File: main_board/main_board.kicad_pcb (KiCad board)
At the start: 2 copper layers, 160 x 110 mm, 143 parts, among them IC1 MP2722GRH-0000-Z, IC2 MP3429GL-Z, IC4 TS921ID, IC5 CY7C65632-28LTXC, IC6 TS921ID, J1 USB3_A, J10 Conn_01x22_Female, J11 501568-0607-TR325, J12 SM04B-XSRS-ETBLFSN, J13 SM10B-XSRS-ETB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

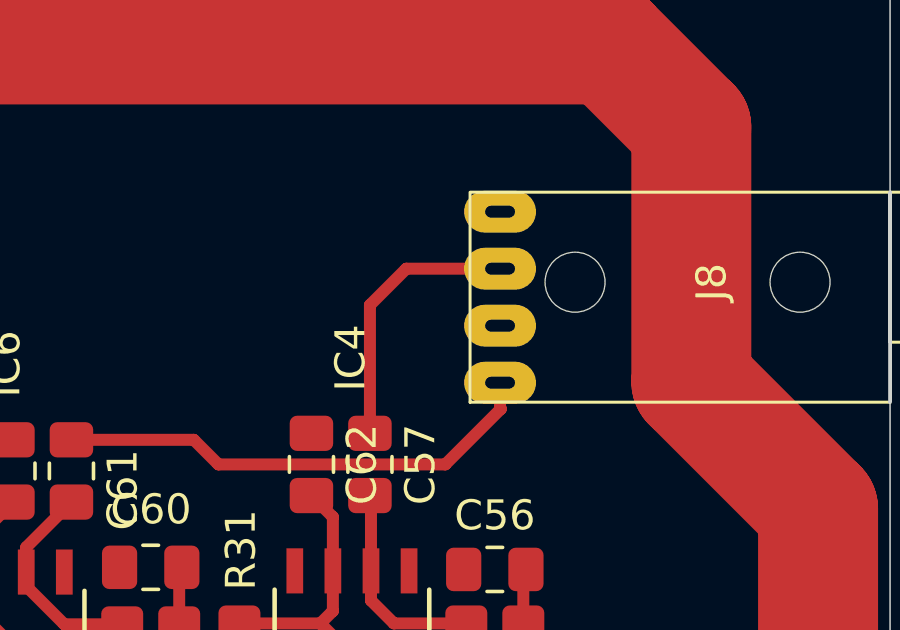
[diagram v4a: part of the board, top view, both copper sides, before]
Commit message: Fix bad jack footprint
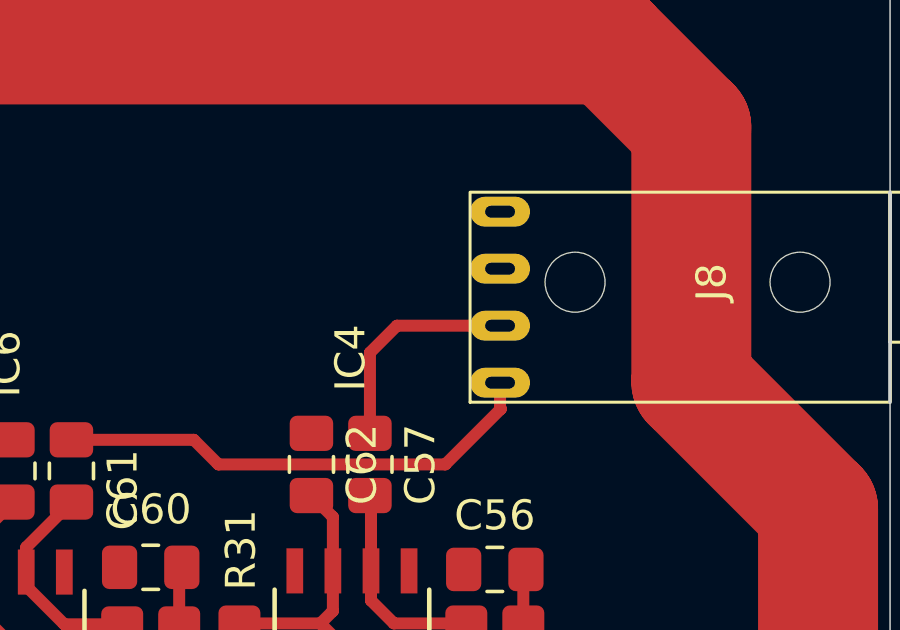
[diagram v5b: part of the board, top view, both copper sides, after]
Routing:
- net Net-(C57-Pad1): track 9.11 -> 7.40 mm
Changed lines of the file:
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@@
 		)
 	)
+	(footprint "000_custom:LUMBERG 1503 16"
+		(layer "F.Cu")
+		(at 184.6 44.025 90)
+		(descr "TRS 3.5mm, horizontal, through-hole, https://www.cuidevices.com/product/resource/pdf/sj1-352xn.pdf")
+		(tags "TRS audio jack stereo horizontal")
+		(property "Reference" "J8"
+			(at 0 -2.65 90)
+			(layer "F.SilkS")
+			(effects
+				(font
+					(size 1 1)
+					(thickness 0.15)
+				)
+			)
+		)
+		(property "Value" "AudioJack3"
+			(at -0.2 -1.6 90)
+			(layer "F.Fab")
+			(effects
+				(font
+					(size 1 1)
+					(thickness 0.15)
+				)
+			)
+		)
+		(property "Footprint" "000_custom:LUMBERG 1503 16"
+			(at 0 0 90)
+			(unlocked yes)
+			(layer "F.Fab")
+			(hide yes)
+			(effects
+				(font
+					(size 1.27 1.27)
+					(thickness 0.15)
+				)
+			)
+		)
+		(property "Datasheet" ""
+			(at 0 0 90)
+			(unlocked yes)
+			(layer "F.Fab")
+			(hide yes)
+			(effects
+				(font
+					(size 1.27 1.27)
+					(thickness 0.15)
+				)
+			)
+		)
+		(property "Description" "Audio Jack, 4 Poles (TRRS)"
+			(at 0 0 90)
+			(unlocked yes)
+			(layer "F.Fab")
+			(hide yes)
+			(effects
+				(font
+					(size 1.27 1.27)
+					(thickness 0.15)
+				)
+			)
+		)
+		(property ki_fp_filters "Jack*")
+		(sheetname "CM5_GPIO")
+		(sheetfile "CM5_GPIO.kicad_sch")
+		(attr through_hole exclude_from_pos_files)
+		(fp_poly
+			(pts
+				(xy -4.000001 -10.7) (xy 3 -10.7) (xy 3 3.3) (xy -4.000001 3.3)
+			)
+			(stroke
+				(width 0.1)
+				(type default)
+			)
+			(fill none)
+			(layer "F.SilkS")
+		)
+		(fp_poly
+			(pts
+				(xy -2 3.3) (xy 3 3.3) (xy 3 6.3) (xy -2 6.3)
+			)
+			(stroke
+				(width 0.1)
+				(type default)
+			)
+			(fill none)
+			(layer "F.SilkS")
+		)
+		(fp_line
+			(start -4.000001 3.3)
+			(end 3 3.3)
+			(stroke
+				(width 0.12)
+				(type solid)
+			)
+			(layer "Edge.Cuts")
+		)
+		(fp_poly
+			(pts
+				(xy -4.150001 -10.85) (xy 3.15 -10.85) (xy 3.15 3.45) (xy -4.150001 3.45)
+			)
+			(stroke
+				(width 0.05)
+				(type default)
+			)
+			(fill none)
+			(layer "F.CrtYd")
+		)
+		(fp_line
+			(start 3 4.5)
+			(end 3 6.3)
+			(stroke
+				(width 0.1)
+				(type solid)
+			)
+			(layer "F.Fab")
+		)
+		(fp_text user "PCB edge"
+			(at -0.4 2.45 90)
+			(unlocked yes)
+			(layer "Dwgs.User")
+			(effects
+				(font
+					(size 1 1)
+					(thickness 0.15)
+				)
+			)
+		)
+		(fp_text user "${REFERENCE}"
+			(at 0 -1.5 90)
+			(layer "F.Fab")
+			(effects
+				(font
+					(size 1 1)
+					(thickness 0.15)
+				)
+			)
+		)
+		(pad "" np_thru_hole circle
+			(at 0 -7.2 90)
+			(size 2 2)
+			(drill 2)
+			(layers "F&B.Cu" "*.Mask")
+		)
+		(pad "" np_thru_hole circle
+			(at 0 0.3 90)
+			(size 2 2)
+			(drill 2)
+			(layers "F&B.Cu" "*.Mask")
+		)
+		(pad "R1" thru_hole oval
+			(at -1.45 -9.7 90)
+			(size 1 2)
+			(drill oval 0.4 1)
+			(layers "*.Cu" "*.Mask")
+			(remove_unused_layers no)
+			(net 216 "Net-(C57-Pad1)")
+			(pintype "passive")
+		)
+		(pad "R2" thru_hole oval
+			(at 0.45 -9.7 90)
+			(size 1 2)
+			(drill oval 0.4 1)
+			(layers "*.Cu" "*.Mask")
+			(remove_unused_layers no)
+			(net 1 "GND")
+			(pintype "passive")
+		)
+		(pad "S" thru_hole oval
+			(at 2.35 -9.7 90)
+			(size 1 2)
+			(drill oval 0.4 1)
+			(layers "*.Cu" "*.Mask")
+			(remove_unused_layers no)
+			(net 1 "GND")
+			(pintype "passive")
+		)
+		(pad "T" thru_hole oval
+			(at -3.35 -9.7 90)
+			(size 1 2)
+			(drill oval 0.4 1)
+			(layers "*.Cu" "*.Mask")
+			(remove_unused_layers no)
+			(net 213 "Net-(C61-Pad1)")
+			(pintype "passive")
+		)
+		(model "${KICAD8_3DMODEL_DIR}/Connector_Audio.3dshapes/Jack_3.5mm_CUI_SJ1-3523N_Horizontal.wrl"
+			(offset
+				(xyz 0 0 0)
+			)
+			(scale
+				(xyz 1 1 1)
+			)
+			(rotate
+				(xyz 0 0 0)
+			)
+		)
+	)
 	(footprint "Capacitor_SMD:C_0805_2012Metric_Pad1.18x1.45mm_HandSolder"
 		(layer "F.Cu")
@@
 		)
 	)
-	(footprint "000_custom:LUMBERG 1503 16"
-		(layer "F.Cu")
-		(at 184.6 44.025 90)
-		(descr "TRS 3.5mm, horizontal, through-hole, https://www.cuidevices.com/product/resource/pdf/sj1-352xn.pdf")
-		(tags "TRS audio jack stereo horizontal")
-		(property "Reference" "J8"
-			(at 0 -2.65 90)
-			(layer "F.SilkS")
-			(effects
-				(font
-					(size 1 1)
-					(thickness 0.15)
-				)
-			)
-		)
-		(property "Value" "AudioJack3"
-			(at -0.2 -1.6 90)
-			(layer "F.Fab")
-			(effects
-				(font
-					(size 1 1)
-					(thickness 0.15)
-				)
-			)
-		)
-		(property "Footprint" "000_custom:LUMBERG 1503 16"
-			(at 0 0 90)
-			(unlocked yes)
-			(layer "F.Fab")
-			(hide yes)
-			(effects
-				(font
-					(size 1.27 1.27)
-					(thickness 0.15)
-				)
-			)
-		)
-		(property "Datasheet" ""
-			(at 0 0 90)
-			(unlocked yes)
-			(layer "F.Fab")
-			(hide yes)
-			(effects
-				(font
-					(size 1.27 1.27)
-					(thickness 0.15)
-				)
-			)
-		)
-		(property "Description" "Audio Jack, 4 Poles (TRRS)"
-			(at 0 0 90)
-			(unlocked yes)
-			(layer "F.Fab")
-			(hide yes)
-			(effects
-				(font
-					(size 1.27 1.27)
-					(thickness 0.15)
-				)
-			)
-		)
-		(property ki_fp_filters "Jack*")
-		(sheetname "CM5_GPIO")
-		(sheetfile "CM5_GPIO.kicad_sch")
-		(attr through_hole exclude_from_pos_files)
-		(fp_poly
-			(pts
-				(xy -4.000001 -10.7) (xy 3 -10.7) (xy 3 3.3) (xy -4.000001 3.3)
-			)
-			(stroke
-				(width 0.1)
-				(type default)
-			)
-			(fill none)
-			(layer "F.SilkS")
-		)
-		(fp_poly
-			(pts
-				(xy -2 3.3) (xy 3 3.3) (xy 3 6.3) (xy -2 6.3)
-			)
-			(stroke
-				(width 0.1)
-				(type default)
-			)
-			(fill none)
-			(layer "F.SilkS")
-		)
-		(fp_line
-			(start -4.000001 3.3)
-			(end 3 3.3)
-			(stroke
-				(width 0.12)
-				(type solid)
-			)
-			(layer "Edge.Cuts")
-		)
-		(fp_poly
-			(pts
-				(xy -4.150001 -10.85) (xy 3.15 -10.85) (xy 3.15 3.45) (xy -4.150001 3.45)
-			)
-			(stroke
-				(width 0.05)
-				(type default)
-			)
-			(fill none)
-			(layer "F.CrtYd")
-		)
-		(fp_line
-			(start 3 4.5)
-			(end 3 6.3)
-			(stroke
-				(width 0.1)
-				(type solid)
-			)
-			(layer "F.Fab")
-		)
-		(fp_text user "PCB edge"
-			(at -0.4 2.45 90)
-			(unlocked yes)
-			(layer "Dwgs.User")
-			(effects
-				(font
-					(size 1 1)
-					(thickness 0.15)
-				)
-			)
-		)
-		(fp_text user "${REFERENCE}"
-			(at 0 -1.5 90)
-			(layer "F.Fab")
-			(effects
-				(font
-					(size 1 1)
-					(thickness 0.15)
-				)
-			)
-		)
-		(pad "" np_thru_hole circle
-			(at 0 -7.2 90)
-			(size 2 2)
-			(drill 2)
-			(layers "F&B.Cu" "*.Mask")
-		)
-		(pad "" np_thru_hole circle
-			(at 0 0.3 90)
-			(size 2 2)
-			(drill 2)
-			(layers "F&B.Cu" "*.Mask")
-		)
-		(pad "R1" thru_hole oval
-			(at 0.45 -9.7 90)
-			(size 1.4 2.4)
-			(drill oval 0.4 1)
-			(layers "*.Cu" "*.Mask")
-			(remove_unused_layers no)
-			(net 216 "Net-(C57-Pad1)")
-			(pintype "passive")
-		)
-		(pad "R2" thru_hole oval
-			(at -1.45 -9.7 90)
-			(size 1.4 2.4)
-			(drill oval 0.4 1)
-			(layers "*.Cu" "*.Mask")
-			(remove_unused_layers no)
-			(net 1 "GND")
-			(pintype "passive")
-		)
-		(pad "S" thru_hole oval
-			(at 2.35 -9.7 90)
-			(size 1.4 2.4)
-			(drill oval 0.4 1)
-			(layers "*.Cu" "*.Mask")
-			(remove_unused_layers no)
-			(net 1 "GND")
-			(pintype "passive")
-		)
-		(pad "T" thru_hole oval
-			(at -3.35 -9.7 90)
-			(size 1.4 2.4)
-			(drill oval 0.4 1)
-			(layers "*.Cu" "*.Mask")
-			(remove_unused_layers no)
-			(net 213 "Net-(C61-Pad1)")
-			(pintype "passive")
-		)
-		(model "${KICAD8_3DMODEL_DIR}/Connector_Audio.3dshapes/Jack_3.5mm_CUI_SJ1-3523N_Horizontal.wrl"
-			(offset
-				(xyz 0 0 0)
-			)
-			(scale
-				(xyz 1 1 1)
-			)
-			(rotate
-				(xyz 0 0 0)
-			)
-		)
-	)
 	(footprint "000_custom:CONN_501568-0607-TR325_MOL"
 		(layer "F.Cu")
@@
 	)
 	(segment
-		(start 170.5625 49.0625)
-		(end 170.5625 44.7875)
+		(start 170.5625 46.375)
+		(end 171.4625 45.475)
 		(width 0.4)
 		(layer "F.Cu")
@@
 	)
 	(segment
-		(start 171.775 43.575)
-		(end 174.9 43.575)
+		(start 170.5625 49.0625)
+		(end 170.5625 46.375)
 		(width 0.4)
 		(layer "F.Cu")
@@
 	)
 	(segment
-		(start 170.5625 44.7875)
-		(end 171.775 43.575)
+		(start 171.4625 45.475)
+		(end 174.9 45.475)
 		(width 0.4)
 		(layer "F.Cu")
